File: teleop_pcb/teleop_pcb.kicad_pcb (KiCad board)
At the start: 2 copper layers, 58.5 x 21 mm, 11 parts

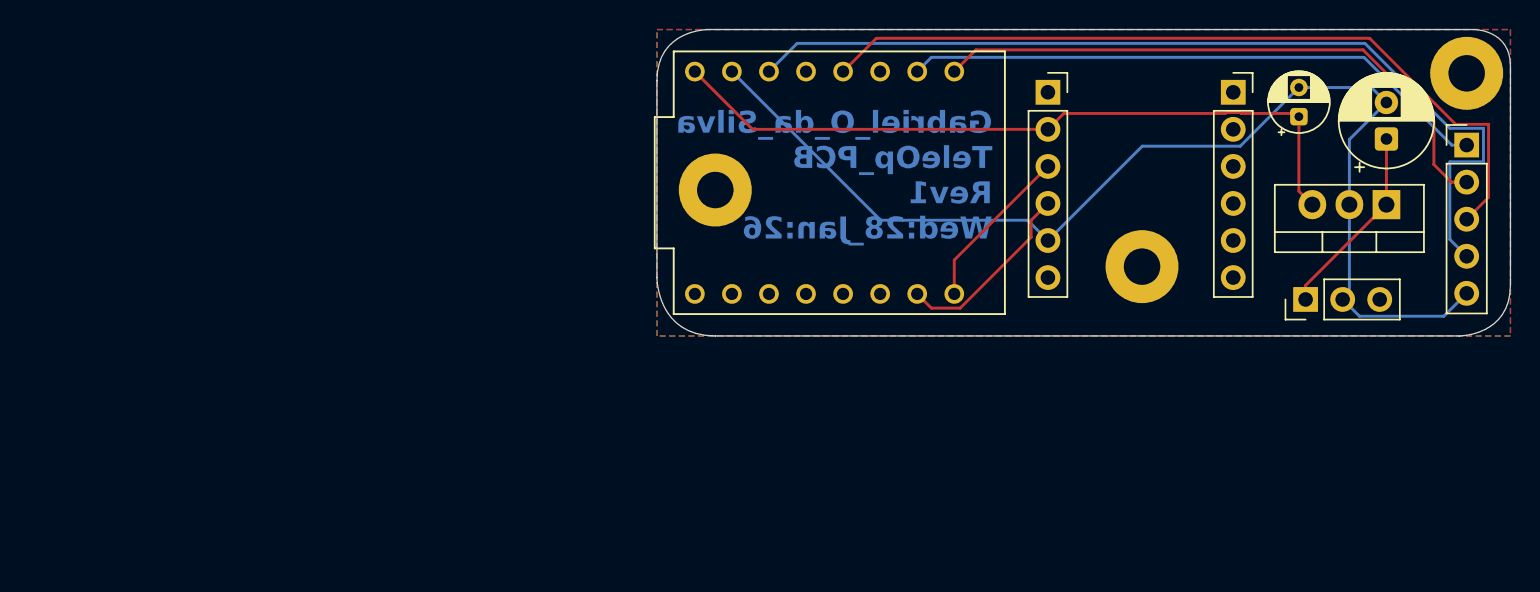
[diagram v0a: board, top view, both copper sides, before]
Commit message: added pin socket rows for teleop pcb
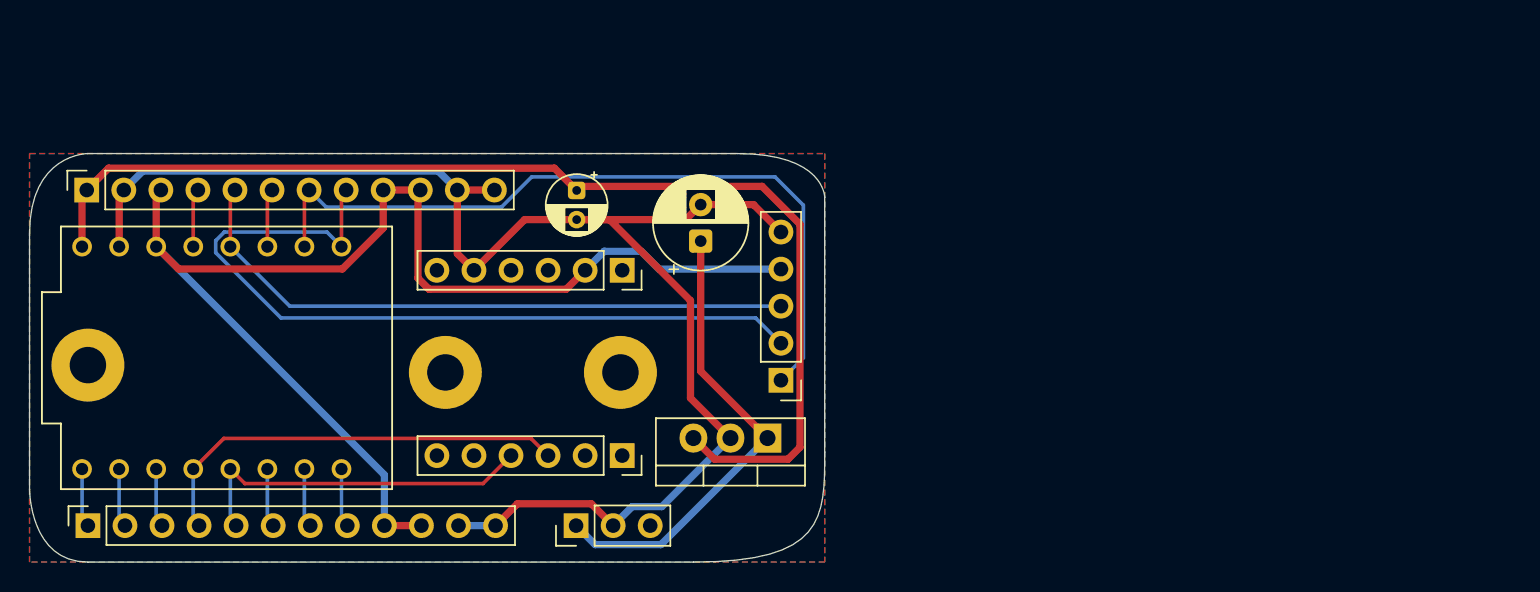
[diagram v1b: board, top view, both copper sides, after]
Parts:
- added Free_Females_Left1: Conn_01x12, Connector_PinSocket_2.54mm:PinSocket_1x12_P2.54mm_Vertical, F.Cu at (57.0, 110.0)
- added Free_Females_Right1: Conn_01x12, Connector_PinSocket_2.54mm:PinSocket_1x12_P2.54mm_Vertical, F.Cu at (56.9, 87.0)
- moved H1 72.6 mm to (57.0, 99.0)
- moved H3 61.5 mm to (93.5, 99.5)
- moved smart_motor1 52.3 mm to (90.5, 110.0)
- moved output_c1 49.8 mm to (90.5, 87.0), turned to -90 degrees
- moved joystick_2axes1 49.7 mm to (104.5, 100.0), turned to 180 degrees
- moved RIGHT_IMU1 48.7 mm to (93.6, 105.2), turned to -90 degrees
- moved input_c1 47.5 mm to (99.0, 90.5)
- moved volt_reg1 45.3 mm to (103.6, 104.0)
- moved ESP32-C3_SuperMini1 43.7 mm to (66.5, 98.5)
- moved LEFT_IMU1 31.6 mm to (93.6, 92.5), turned to -90 degrees
- moved H2 22.3 mm to (81.5, 99.5)
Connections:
- ESP32-C3_SuperMini1 pad 10: unconnected-(ESP32-C3_SuperMini1-GPIO10-Pad10) -> /.
- ESP32-C3_SuperMini1 pad 2: unconnected-(ESP32-C3_SuperMini1-GPIO2-Pad2) -> /.
- ESP32-C3_SuperMini1 pad 20: /TX_IMU -> /.
- ESP32-C3_SuperMini1 pad 21: /RX_IMU -> /.
- ESP32-C3_SuperMini1 pad 4: unconnected-(ESP32-C3_SuperMini1-GPIO4-Pad4) -> /.
- ESP32-C3_SuperMini1 pad 5: unconnected-(ESP32-C3_SuperMini1-GPIO5-Pad5) -> /.
- ESP32-C3_SuperMini1 pad 6: unconnected-(ESP32-C3_SuperMini1-GPIO6-Pad6) -> /.
- ESP32-C3_SuperMini1 pad 7: unconnected-(ESP32-C3_SuperMini1-GPIO7-Pad7) -> /.
- ESP32-C3_SuperMini1 pad 8: unconnected-(ESP32-C3_SuperMini1-GPIO8-Pad8) -> /SDA
- ESP32-C3_SuperMini1 pad 9: unconnected-(ESP32-C3_SuperMini1-GPIO9-Pad9) -> /SCL
- LEFT_IMU1 pad 2: /5V0 -> /3V3
- LEFT_IMU1 pad 3: /RX_IMU -> unconnected-(LEFT_IMU1-RX-Pad3)
- LEFT_IMU1 pad 4: /TX_IMU -> unconnected-(LEFT_IMU1-TX-Pad4)
- RIGHT_IMU1 pad 3: unconnected-(RIGHT_IMU1-Pin_3-Pad3) -> /SDA
- RIGHT_IMU1 pad 4: unconnected-(RIGHT_IMU1-Pin_4-Pad4) -> /SCL
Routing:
- net /.: track 0.00 -> 32.3 mm
- net /SDA: track 0.00 -> 29.7 mm
- net /5V0: track 50.0 -> 78.9 mm
- net /SCL: track 0.00 -> 24.5 mm
- net GND: track 78.8 -> 103.2 mm
- net /3V3: track 63.7 -> 87.5 mm
- net /7V4: track 13.8 -> 32.8 mm
- net /RY: track 41.2 -> 55.4 mm
- net /TX_IMU: track 13.0 -> 0.00 mm
- net /SW: track 40.6 -> 52.7 mm
- net /RX_IMU: track 11.4 -> 0.00 mm
- net /RX: track 54.7 -> 43.4 mm
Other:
- board size 58.5 x 21 mm -> 54.5 x 28 mm
- board text added: "Gabriel_O._da_Silva TeleOp_PCB Rev3 1_Feb_2026"
- board text removed: "Gabriel_O_da_Silva TeleOp_PCB Rev1 Wed:28_Jan:26"
